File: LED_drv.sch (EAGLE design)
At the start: 59 parts, among them IC1 LM3409, IC2 LM393D, Q2 IPD50R380, T1 IRLR9343PBF, T2 BCX56, T4 BT169, T5 BT169, T6 TLP266J

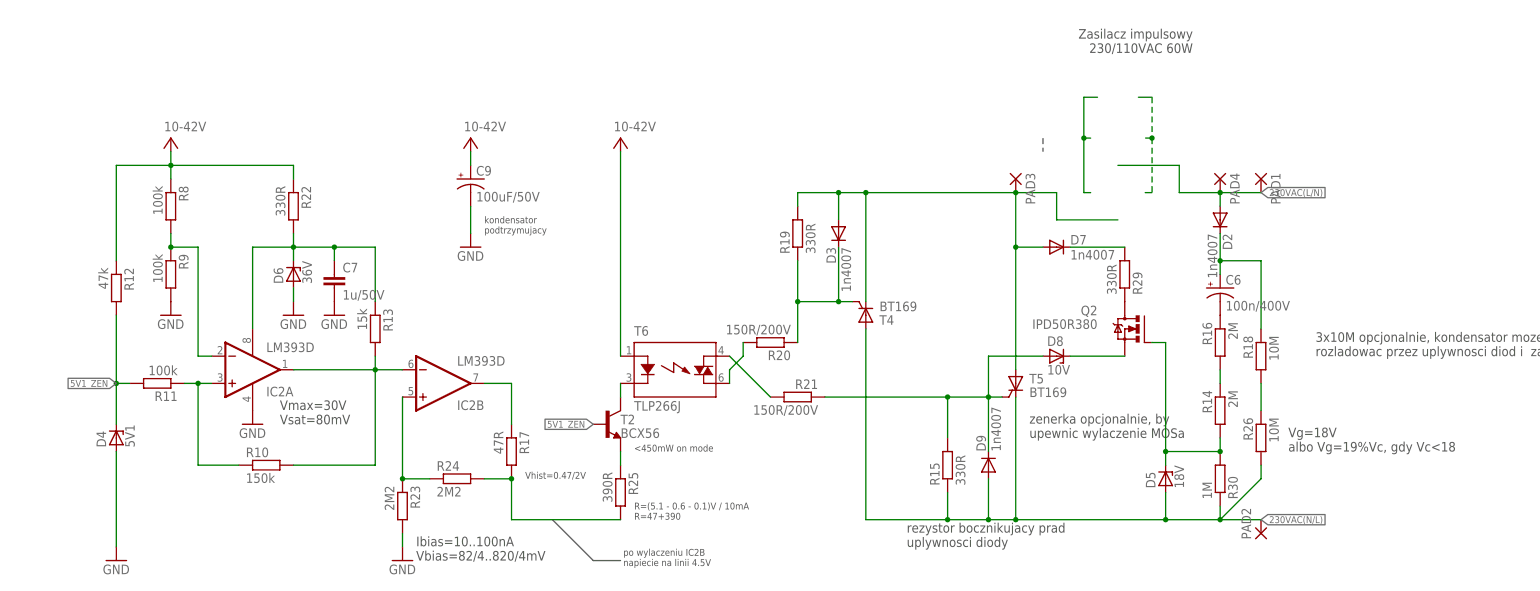
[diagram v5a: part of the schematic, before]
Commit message: key side PCB layout
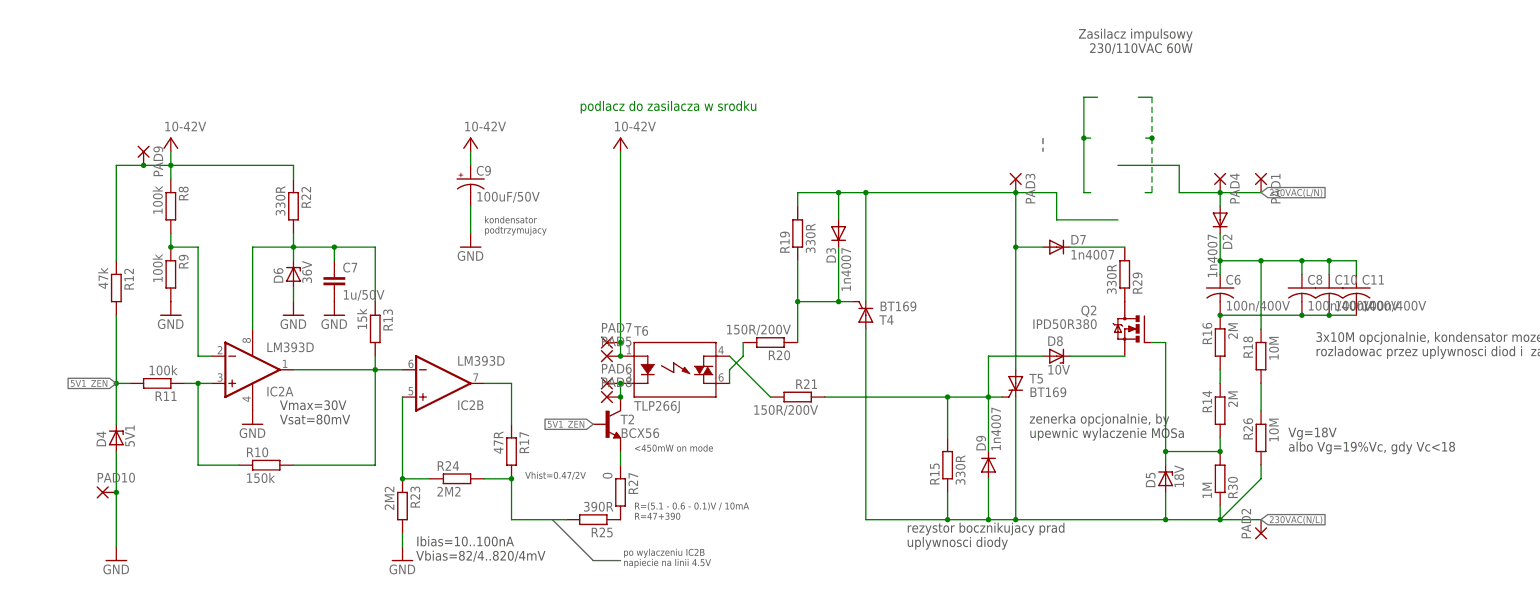
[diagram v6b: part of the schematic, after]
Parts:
- added C10, C11, C8: 100n/400V, rcl:C-US075-032X103
- added PAD10, PAD5, PAD6, PAD7, PAD8, PAD9: (no value), wirepad:SMD2
- added R27: 0, resistor:R-EU_R0805
- C6: device rcl:CPOL-USE3.5-8 -> rcl:C-US075-032X103
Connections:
- new net N$34: C10.2, C11.2, C6.2, C8.2, R16.1
- net GND: now also PAD10.P
- net N$12: now also R25.1, R27.2; no longer C6.-, R16.1
- net N$14: now also C10.1, C11.1, C6.1, C8.1; no longer C6.+
- net N$22: now also R27.1; no longer R25.1
- net N$27: now also PAD6.P, PAD8.P
- net V+: now also PAD5.P, PAD7.P, PAD9.P
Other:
- note added: "podlacz do zasilacza w srodku"
- moved on the sheet: R25
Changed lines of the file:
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@@
 <part name="R11" library="resistor" deviceset="R-EU_" device="R0805" value="100k"/>
 <part name="R12" library="resistor" deviceset="R-EU_" device="R0805" value="47k"/>
-<part name="C6" library="rcl" deviceset="CPOL-US" device="E3.5-8" value="100n/400V"/>
+<part name="C6" library="rcl" deviceset="C-US" device="075-032X103" value="100n/400V"/>
 <part name="D2" library="diode" deviceset="DIODE-" device="DO-214AC" value="1n4007"/>
 <part name="T5" library="miscrel" deviceset="BT169" device=""/>
@@
 <part name="R18" library="rcl" deviceset="R-EU_" device="R1206" value="10M"/>
 <part name="R26" library="rcl" deviceset="R-EU_" device="R1206" value="10M"/>
+<part name="PAD5" library="wirepad" deviceset="SMD2" device=""/>
+<part name="PAD6" library="wirepad" deviceset="SMD2" device=""/>
+<part name="C8" library="rcl" deviceset="C-US" device="075-032X103" value="100n/400V"/>
+<part name="C10" library="rcl" deviceset="C-US" device="075-032X103" value="100n/400V"/>
+<part name="C11" library="rcl" deviceset="C-US" device="075-032X103" value="100n/400V"/>
+<part name="PAD7" library="wirepad" deviceset="SMD2" device=""/>
+<part name="PAD8" library="wirepad" deviceset="SMD2" device=""/>
+<part name="PAD9" library="wirepad" deviceset="SMD2" device=""/>
+<part name="PAD10" library="wirepad" deviceset="SMD2" device=""/>
+<part name="R27" library="resistor" deviceset="R-EU_" device="R0805" value="0"/>
 </parts>
 <sheets>
@@
 <text x="393.7" y="-22.86" size="1.778" layer="97">zenerka opcjonalnie, by
 upewnic wylaczenie MOSa</text>
+<text x="309.88" y="38.1" size="1.778" layer="91">podlacz do zasilacza w srodku</text>
 </plain>
 <instances>
@@
 <instance part="R23" gate="G$1" x="276.86" y="-35.56" rot="R270"/>
 <instance part="T2" gate="G$1" x="317.5" y="-20.32"/>
-<instance part="R25" gate="G$1" x="317.5" y="-33.02" rot="R270"/>
+<instance part="R25" gate="G$1" x="312.42" y="-38.1" rot="R180"/>
 <instance part="SUPPLY3" gate="1" x="317.5" y="33.02"/>
 <instance part="R17" gate="G$1" x="297.18" y="-25.4" rot="R270"/>
@@
 <instance part="R18" gate="G$1" x="436.88" y="-7.62" rot="MR270"/>
 <instance part="R26" gate="G$1" x="436.88" y="-22.86" rot="MR270"/>
+<instance part="PAD5" gate="1" x="314.96" y="-7.62"/>
+<instance part="PAD6" gate="1" x="314.96" y="-12.7"/>
+<instance part="C8" gate="G$1" x="444.5" y="5.08"/>
+<instance part="C10" gate="G$1" x="449.58" y="5.08"/>
+<instance part="C11" gate="G$1" x="454.66" y="5.08"/>
+<instance part="PAD7" gate="1" x="314.96" y="-5.08"/>
+<instance part="PAD8" gate="1" x="314.96" y="-15.24"/>
+<instance part="PAD9" gate="1" x="228.6" y="30.48" rot="R270"/>
+<instance part="PAD10" gate="1" x="220.98" y="-33.02"/>
+<instance part="R27" gate="G$1" x="317.5" y="-33.02" rot="R270"/>
 </instances>
 <busses>
@@
 <segment>
 <pinref part="D4" gate="G$1" pin="A"/>
-<wire x1="223.52" y1="-25.4" x2="223.52" y2="-43.18" width="0.1524" layer="91"/>
+<wire x1="223.52" y1="-25.4" x2="223.52" y2="-33.02" width="0.1524" layer="91"/>
 <pinref part="GND11" gate="1" pin="GND"/>
+<pinref part="PAD10" gate="1" pin="P"/>
+<wire x1="223.52" y1="-33.02" x2="223.52" y2="-43.18" width="0.1524" layer="91"/>
+<junction x="223.52" y="-33.02"/>
 </segment>
 <segment>
@@
 </segment>
 </net>
-<net name="N$12" class="0">
-<segment>
-<pinref part="R16" gate="G$1" pin="1"/>
-<pinref part="C6" gate="G$1" pin="-"/>
-</segment>
-</net>
 <net name="N$14" class="0">
 <segment>
-<pinref part="C6" gate="G$1" pin="+"/>
+<pinref part="C6" gate="G$1" pin="1"/>
 <pinref part="D2" gate="G$1" pin="C"/>
 <wire x1="429.26" y1="7.62" x2="429.26" y2="10.16" width="0.1524" layer="91"/>
@@
 <junction x="429.26" y="10.16"/>
 <pinref part="R18" gate="G$1" pin="1"/>
+<pinref part="C8" gate="G$1" pin="1"/>
+<wire x1="444.5" y1="7.62" x2="444.5" y2="10.16" width="0.1524" layer="91"/>
+<wire x1="444.5" y1="10.16" x2="436.88" y2="10.16" width="0.1524" layer="91"/>
+<junction x="436.88" y="10.16"/>
+<pinref part="C10" gate="G$1" pin="1"/>
+<wire x1="444.5" y1="10.16" x2="449.58" y2="10.16" width="0.1524" layer="91"/>
+<wire x1="449.58" y1="10.16" x2="449.58" y2="7.62" width="0.1524" layer="91"/>
+<junction x="444.5" y="10.16"/>
+<pinref part="C11" gate="G$1" pin="1"/>
+<wire x1="449.58" y1="10.16" x2="454.66" y2="10.16" width="0.1524" layer="91"/>
+<wire x1="454.66" y1="10.16" x2="454.66" y2="7.62" width="0.1524" layer="91"/>
+<junction x="449.58" y="10.16"/>
 </segment>
 </net>
@@
 <pinref part="R12" gate="G$1" pin="1"/>
 <wire x1="223.52" y1="10.16" x2="223.52" y2="27.94" width="0.1524" layer="91"/>
-<wire x1="223.52" y1="27.94" x2="233.68" y2="27.94" width="0.1524" layer="91"/>
+<wire x1="223.52" y1="27.94" x2="228.6" y2="27.94" width="0.1524" layer="91"/>
+<wire x1="228.6" y1="27.94" x2="233.68" y2="27.94" width="0.1524" layer="91"/>
 <wire x1="233.68" y1="27.94" x2="256.54" y2="27.94" width="0.1524" layer="91"/>
 <pinref part="R8" gate="G$1" pin="1"/>
@@
 <pinref part="SUPPLY1" gate="1" pin="V+"/>
 <wire x1="233.68" y1="30.48" x2="233.68" y2="27.94" width="0.1524" layer="91"/>
+<pinref part="PAD9" gate="1" pin="P"/>
+<junction x="228.6" y="27.94"/>
 </segment>
 <segment>
 <pinref part="T6" gate="G$1" pin="A"/>
-<wire x1="317.5" y1="-7.62" x2="317.5" y2="30.48" width="0.1524" layer="91"/>
+<wire x1="317.5" y1="-7.62" x2="317.5" y2="-5.08" width="0.1524" layer="91"/>
 <pinref part="SUPPLY3" gate="1" pin="V+"/>
+<pinref part="PAD5" gate="1" pin="P"/>
+<junction x="317.5" y="-7.62"/>
+<pinref part="PAD7" gate="1" pin="P"/>
+<wire x1="317.5" y1="-5.08" x2="317.5" y2="30.48" width="0.1524" layer="91"/>
+<junction x="317.5" y="-5.08"/>
 </segment>
 <segment>
@@
 <segment>
 <pinref part="R25" gate="G$1" pin="2"/>
-<wire x1="317.5" y1="-38.1" x2="297.18" y2="-38.1" width="0.1524" layer="91"/>
+<wire x1="307.34" y1="-38.1" x2="297.18" y2="-38.1" width="0.1524" layer="91"/>
 <pinref part="R17" gate="G$1" pin="2"/>
 <wire x1="297.18" y1="-30.48" x2="297.18" y2="-38.1" width="0.1524" layer="91"/>
@@
 <segment>
 <pinref part="T2" gate="G$1" pin="E"/>
-<pinref part="R25" gate="G$1" pin="1"/>
 <wire x1="317.5" y1="-25.4" x2="317.5" y2="-27.94" width="0.1524" layer="91"/>
+<pinref part="R27" gate="G$1" pin="1"/>
 </segment>
 </net>
@@
 <pinref part="T2" gate="G$1" pin="C"/>
 <wire x1="317.5" y1="-12.7" x2="317.5" y2="-15.24" width="0.1524" layer="91"/>
+<pinref part="PAD6" gate="1" pin="P"/>
+<junction x="317.5" y="-12.7"/>
+<pinref part="PAD8" gate="1" pin="P"/>
+<junction x="317.5" y="-15.24"/>
 </segment>
 </net>
@@
 </segment>
 </net>
+<net name="N$34" class="0">
+<segment>
+<pinref part="C11" gate="G$1" pin="2"/>
+<pinref part="C10" gate="G$1" pin="2"/>
+<wire x1="454.66" y1="0" x2="449.58" y2="0" width="0.1524" layer="91"/>
+<pinref part="C8" gate="G$1" pin="2"/>
+<wire x1="449.58" y1="0" x2="444.5" y2="0" width="0.1524" layer="91"/>
+<junction x="449.58" y="0"/>
+<pinref part="R16" gate="G$1" pin="1"/>
+<pinref part="C6" gate="G$1" pin="2"/>
+<wire x1="444.5" y1="0" x2="429.26" y2="0" width="0.1524" layer="91"/>
+<junction x="444.5" y="0"/>
+<junction x="429.26" y="0"/>
+</segment>
+</net>
+<net name="N$12" class="0">
+<segment>
+<pinref part="R25" gate="G$1" pin="1"/>
+<pinref part="R27" gate="G$1" pin="2"/>
+</segment>
+</net>
